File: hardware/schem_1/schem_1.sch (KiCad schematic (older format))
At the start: 37 parts, among them J1 OV7670_Conn_01x24_MountingPin, J2 Micro_SD_Card, J3 FRONT_PCB_CONNECTOR, J4 BG300-04-X-X-A_REVC, J6 BACK_PCB_CONNECTOR, SW1 BTN_BOOT, SW2 ESP32_RESET, U1 ESP32-WROVER-E-JC

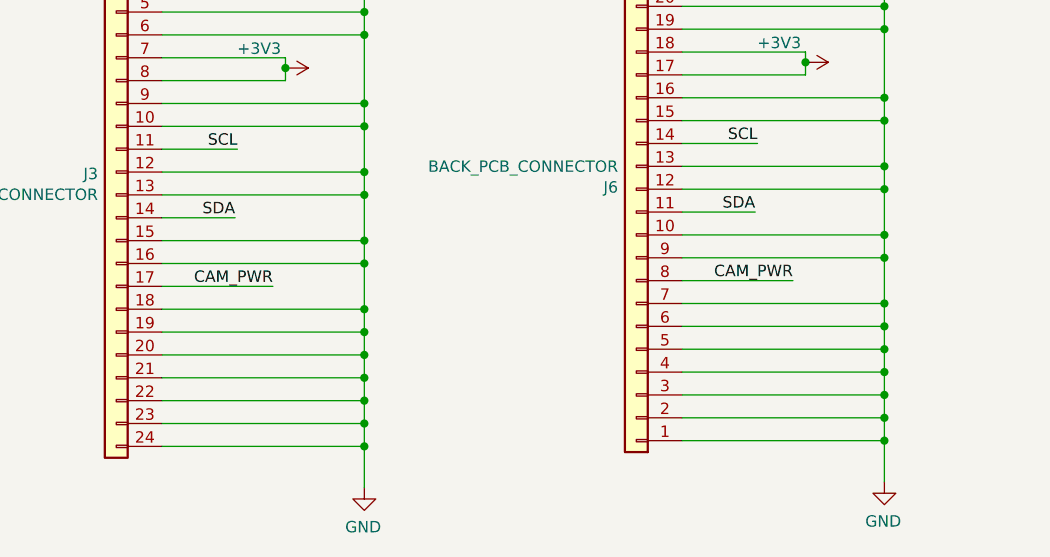
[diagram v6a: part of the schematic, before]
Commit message: finish first round tracks and filled zones for front PCB. Do silk screen
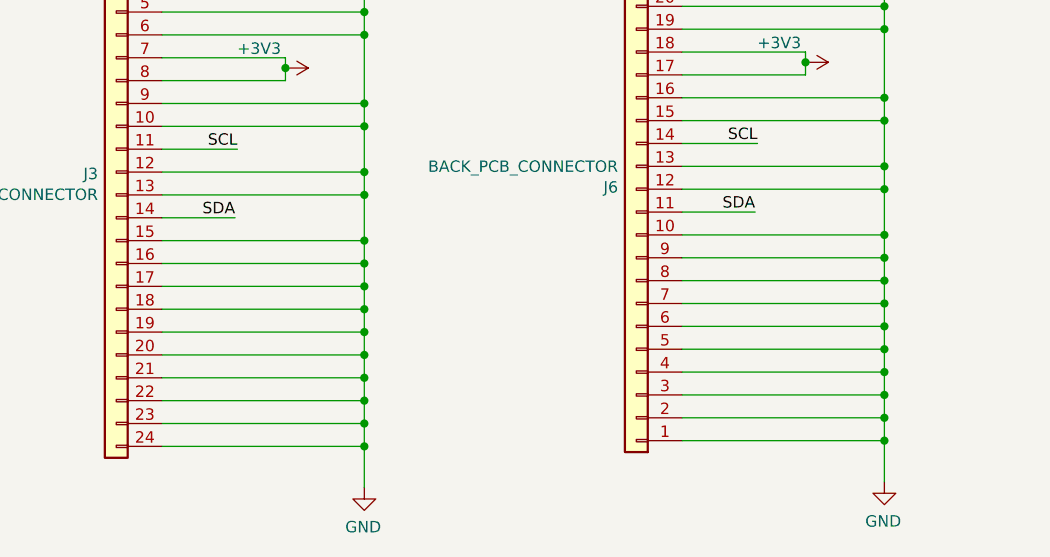
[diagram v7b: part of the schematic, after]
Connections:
- wire segments 215 -> 217
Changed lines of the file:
@@
 Text Notes 2225 5575 0    79   ~ 0
 MicroSD Card
-Wire Wire Line
-	7435 7265 7435 7315
-$Comp
-L power:GND #PWR0102
-U 1 1 60D682C7
-P 7435 7315
-F 0 "#PWR0102" H 7435 7065 50  0001 C CNN
-F 1 "GND" H 7440 7142 50  0000 C CNN
-F 2 "" H 7435 7315 50  0001 C CNN
-F 3 "" H 7435 7315 50  0001 C CNN
-	1    7435 7315
-	1    0    0    -1
-$EndComp
 NoConn ~ 10100 1225
 NoConn ~ 10100 1325
-Text Label 7635 7165 2    50   ~ 0
-U0RXD
-Text Label 7635 7065 2    50   ~ 0
-U0TXD
-Wire Wire Line
-	7635 7165 7335 7165
-Wire Wire Line
-	7635 7065 7335 7065
-Wire Wire Line
-	7335 7265 7435 7265
 $Comp
 L Mechanical:MountingHole H1
@@
 Wire Wire Line
 	2750 8735 2750 8680
-Wire Wire Line
-	2210 9635 2695 9635
 $Comp
 L Connector_Generic:Conn_01x24 J3
@@
 	-1   0    0    -1
 $EndComp
-Text Label 2695 9635 2    50   ~ 0
-CAM_PWR
 Connection ~ 2750 8680
 Wire Wire Line
@@
 	2210 9735 3095 9735
 Wire Wire Line
-	3095 9535 3095 9735
+	3095 9535 3095 9635
 Connection ~ 3095 9735
 Wire Wire Line
@@
 Wire Wire Line
 	5025 8710 5025 8655
-Wire Wire Line
-	4485 9610 4970 9610
-Text Label 4970 9610 2    50   ~ 0
-CAM_PWR
 Connection ~ 5025 8655
 Wire Wire Line
@@
 	4485 9710 5370 9710
 Wire Wire Line
-	5370 9510 5370 9710
+	5370 9510 5370 9610
 Connection ~ 5370 9710
 Wire Wire Line
@@
 Wire Wire Line
 	5370 10310 5370 10490
+Wire Wire Line
+	6800 2300 6335 2300
+Connection ~ 6800 2300
+Wire Wire Line
+	7335 6965 7635 6965
+Text Label 7390 6965 0    50   ~ 0
+5V_USB_SC
 $Comp
 L BG300-04-X-X-A_REVC:BG300-04-X-X-A_REVC J4
@@
 	-1   0    0    1
 $EndComp
-Text Label 7390 6965 0    50   ~ 0
-5V_USB_SC
-Wire Wire Line
-	7335 6965 7635 6965
-Wire Wire Line
-	6800 2300 6335 2300
-Connection ~ 6800 2300
+Wire Wire Line
+	7335 7265 7435 7265
+Wire Wire Line
+	7635 7065 7335 7065
+Wire Wire Line
+	7635 7165 7335 7165
+Text Label 7635 7065 2    50   ~ 0
+U0TXD
+Text Label 7635 7165 2    50   ~ 0
+U0RXD
+$Comp
+L power:GND #PWR0102
+U 1 1 60D682C7
+P 7435 7315
+F 0 "#PWR0102" H 7435 7065 50  0001 C CNN
+F 1 "GND" H 7440 7142 50  0000 C CNN
+F 2 "" H 7435 7315 50  0001 C CNN
+F 3 "" H 7435 7315 50  0001 C CNN
+	1    7435 7315
+	1    0    0    -1
+$EndComp
+Wire Wire Line
+	7435 7265 7435 7315
+Wire Wire Line
+	2210 9635 3095 9635
+Connection ~ 3095 9635
+Wire Wire Line
+	3095 9635 3095 9735
+Wire Wire Line
+	4485 9610 5370 9610
+Connection ~ 5370 9610
+Wire Wire Line
+	5370 9610 5370 9710
 $EndSCHEMATC

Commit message: update to latest gerbers, update project plan
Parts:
- C1: LCSC (none) -> C16780
- C25, C6: LCSC (none) -> C15849
- C26, C4, C5: LCSC (none) -> C268011
- C3: LCSC (none) -> C1644
- R1, R3, R6: LCSC (none) -> C23162
- R12, R13, R14, R15: LCSC (none) -> C25819
- R2, R8: LCSC (none) -> C25804
- R26, R27: LCSC (none) -> C22978
- R4: LCSC (none) -> C21189
- R7: LCSC (none) -> C21190
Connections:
- wire segments 217 -> 218
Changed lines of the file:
@@
 F 2 "Resistor_SMD:R_0603_1608Metric" V 10280 5525 50  0001 C CNN
 F 3 "~" H 10350 5525 50  0001 C CNN
+F 4 "C23162" V 10350 5525 50  0001 C CNN "LCSC"
 	1    10350 5525
 	0    -1   -1   0
@@
 F 2 "Capacitor_SMD:C_0603_1608Metric" H 10150 5775 50  0001 C CNN
 F 3 "~" H 10150 5775 50  0001 C CNN
+F 4 "C268011" H 10150 5775 50  0001 C CNN "LCSC"
 	1    10150 5775
 	1    0    0    -1
@@
 F 2 "Resistor_SMD:R_0603_1608Metric" V 10205 4350 50  0001 C CNN
 F 3 "~" H 10275 4350 50  0001 C CNN
+F 4 "C23162" V 10275 4350 50  0001 C CNN "LCSC"
 	1    10275 4350
 	0    -1   -1   0
@@
 F 2 "Resistor_SMD:R_0603_1608Metric" V 10205 4650 50  0001 C CNN
 F 3 "~" H 10275 4650 50  0001 C CNN
+F 4 "C23162" V 10275 4650 50  0001 C CNN "LCSC"
 	1    10275 4650
 	0    -1   -1   0
@@
 F 2 "Resistor_SMD:R_0603_1608Metric" V 5705 5575 50  0001 C CNN
 F 3 "~" H 5775 5575 50  0001 C CNN
+F 4 "C25804" H 5775 5575 50  0001 C CNN "LCSC"
 	1    5775 5575
 	1    0    0    -1
@@
 F 2 "Capacitor_SMD:C_0603_1608Metric" H 5775 6125 50  0001 C CNN
 F 3 "~" H 5775 6125 50  0001 C CNN
+F 4 "C15849" H 5775 6125 50  0001 C CNN "LCSC"
 	1    5775 6125
 	1    0    0    -1
@@
 U 1 1 60A5CEA1
 P 1050 6150
-F 0 "R11" V 1000 6000 50  0000 C CNN
+F 0 "R11" V 1130 6135 50  0000 C CNN
 F 1 "DNC" V 1050 6150 50  0000 C CNN
 F 2 "Resistor_SMD:R_0603_1608Metric" V 980 6150 50  0001 C CNN
@@
 U 1 1 60A622E2
 P 1050 6250
-F 0 "R12" V 1000 6100 50  0000 C CNN
-F 1 "47K" V 1050 6250 50  0000 C CNN
+F 0 "R12" V 1050 6070 50  0000 C CNN
+F 1 "47K" V 1035 6570 50  0000 C CNN
 F 2 "Resistor_SMD:R_0603_1608Metric" V 980 6250 50  0001 C CNN
 F 3 "~" H 1050 6250 50  0001 C CNN
+F 4 "C25819" V 1050 6250 50  0001 C CNN "LCSC"
 	1    1050 6250
 	0    -1   -1   0
@@
 U 1 1 60A6727D
 P 1050 6350
-F 0 "R13" V 1000 6200 50  0000 C CNN
-F 1 "47K" V 1050 6350 50  0000 C CNN
+F 0 "R13" V 1045 6160 50  0000 C CNN
+F 1 "47K" V 1035 6685 50  0000 C CNN
 F 2 "Resistor_SMD:R_0603_1608Metric" V 980 6350 50  0001 C CNN
 F 3 "~" H 1050 6350 50  0001 C CNN
+F 4 "C25819" V 1050 6350 50  0001 C CNN "LCSC"
 	1    1050 6350
 	0    -1   -1   0
@@
 U 1 1 60A78F24
 P 1050 6750
-F 0 "R14" V 1000 6600 50  0000 C CNN
-F 1 "47K" V 1050 6750 50  0000 C CNN
+F 0 "R14" V 1050 6570 50  0000 C CNN
+F 1 "47K" V 1050 7045 50  0000 C CNN
 F 2 "Resistor_SMD:R_0603_1608Metric" V 980 6750 50  0001 C CNN
 F 3 "~" H 1050 6750 50  0001 C CNN
+F 4 "C25819" V 1050 6750 50  0001 C CNN "LCSC"
 	1    1050 6750
 	0    -1   -1   0
@@
 U 1 1 60A7E9CE
 P 1050 6850
-F 0 "R15" V 1000 6700 50  0000 C CNN
-F 1 "47K" V 1050 6850 50  0000 C CNN
+F 0 "R15" V 1050 6640 50  0000 C CNN
+F 1 "47K" V 1055 7110 50  0000 C CNN
 F 2 "Resistor_SMD:R_0603_1608Metric" V 980 6850 50  0001 C CNN
 F 3 "~" H 1050 6850 50  0001 C CNN
+F 4 "C25819" V 1050 6850 50  0001 C CNN "LCSC"
 	1    1050 6850
 	0    -1   -1   0
@@
 F 2 "Capacitor_SMD:C_0603_1608Metric" H 10650 1925 50  0001 C CNN
 F 3 "~" H 10650 1925 50  0001 C CNN
+F 4 "C1644" V 10650 1925 50  0001 C CNN "LCSC"
 	1    10650 1925
 	0    1    1    0
@@
 F 2 "Capacitor_SMD:C_0603_1608Metric" H 10750 2525 50  0001 C CNN
 F 3 "~" H 10750 2525 50  0001 C CNN
+F 4 "C268011" V 10750 2525 50  0001 C CNN "LCSC"
 	1    10750 2525
 	0    1    1    0
@@
 F 2 "Resistor_SMD:R_0603_1608Metric" V 10580 2825 50  0001 C CNN
 F 3 "~" H 10650 2825 50  0001 C CNN
+F 4 "C21190" V 10650 2825 50  0001 C CNN "LCSC"
 	1    10650 2825
 	0    1    1    0
@@
 F 2 "Resistor_SMD:R_0603_1608Metric" H 10550 1625 50  0001 C CNN
 F 3 "~" H 10550 1625 50  0001 C CNN
+F 4 "C21189" H 10550 1625 50  0001 C CNN "LCSC"
 	1    10550 1625
 	-1   0    0    1
@@
 F 2 "Resistor_SMD:R_0603_1608Metric" H 5850 4525 50  0001 C CNN
 F 3 "~" H 5850 4525 50  0001 C CNN
+F 4 "C25804" H 5850 4525 50  0001 C CNN "LCSC"
 	1    5850 4525
 	1    0    0    -1
@@
 F 2 "Capacitor_SMD:C_0603_1608Metric" H 2775 1150 50  0001 C CNN
 F 3 "~" H 2775 1150 50  0001 C CNN
+F 4 "C268011" H 2775 1150 50  0001 C CNN "LCSC"
 	1    2775 1150
 	-1   0    0    -1
@@
 F 2 "Capacitor_SMD:C_0603_1608Metric" H 2400 1150 50  0001 C CNN
 F 3 "~" H 2400 1150 50  0001 C CNN
+F 4 "C15849" H 2400 1150 50  0001 C CNN "LCSC"
 	1    2400 1150
 	-1   0    0    -1
@@
 F 2 "Capacitor_SMD:C_0805_2012Metric" H 2025 1150 50  0001 C CNN
 F 3 "~" H 2025 1150 50  0001 C CNN
+F 4 "C16780" H 2025 1150 50  0001 C CNN "LCSC"
 	1    2025 1150
 	-1   0    0    -1
@@
 F 2 "Resistor_SMD:R_0603_1608Metric" H 2675 2150 50  0001 C CNN
 F 3 "~" H 2675 2150 50  0001 C CNN
+F 4 "C22978" V 2675 2150 50  0001 C CNN "LCSC"
 	1    2675 2150
 	0    -1   -1   0
@@
 F 2 "Resistor_SMD:R_0603_1608Metric" H 5100 1750 50  0001 C CNN
 F 3 "~" H 5100 1750 50  0001 C CNN
+F 4 "C22978" V 5100 1750 50  0001 C CNN "LCSC"
 	1    5100 1750
 	0    -1   -1   0
@@
 Wire Wire Line
 	5370 9610 5370 9710
+$Comp
+L power:GND #PWR0109
+U 1 1 60D9C5B0
+P 14155 5355
+F 0 "#PWR0109" H 14155 5105 50  0001 C CNN
+F 1 "GND" H 14160 5182 50  0000 C CNN
+F 2 "" H 14155 5355 50  0001 C CNN
+F 3 "" H 14155 5355 50  0001 C CNN
+	1    14155 5355
+	1    0    0    -1
+$EndComp
+Wire Wire Line
+	14155 5280 14155 5355
+$Comp
+L power:PWR_FLAG #FLG0103
+U 1 1 60DBCB75
+P 14155 5280
+F 0 "#FLG0103" H 14155 5355 50  0001 C CNN
+F 1 "PWR_FLAG" V 14155 5408 50  0000 L CNN
+F 2 "" H 14155 5280 50  0001 C CNN
+F 3 "~" H 14155 5280 50  0001 C CNN
+	1    14155 5280
+	0    1    1    0
+$EndComp
 $EndSCHEMATC
